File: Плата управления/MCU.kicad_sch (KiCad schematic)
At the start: 19 parts, among them U4 STM32F767VITx, U7 ASEMB-10

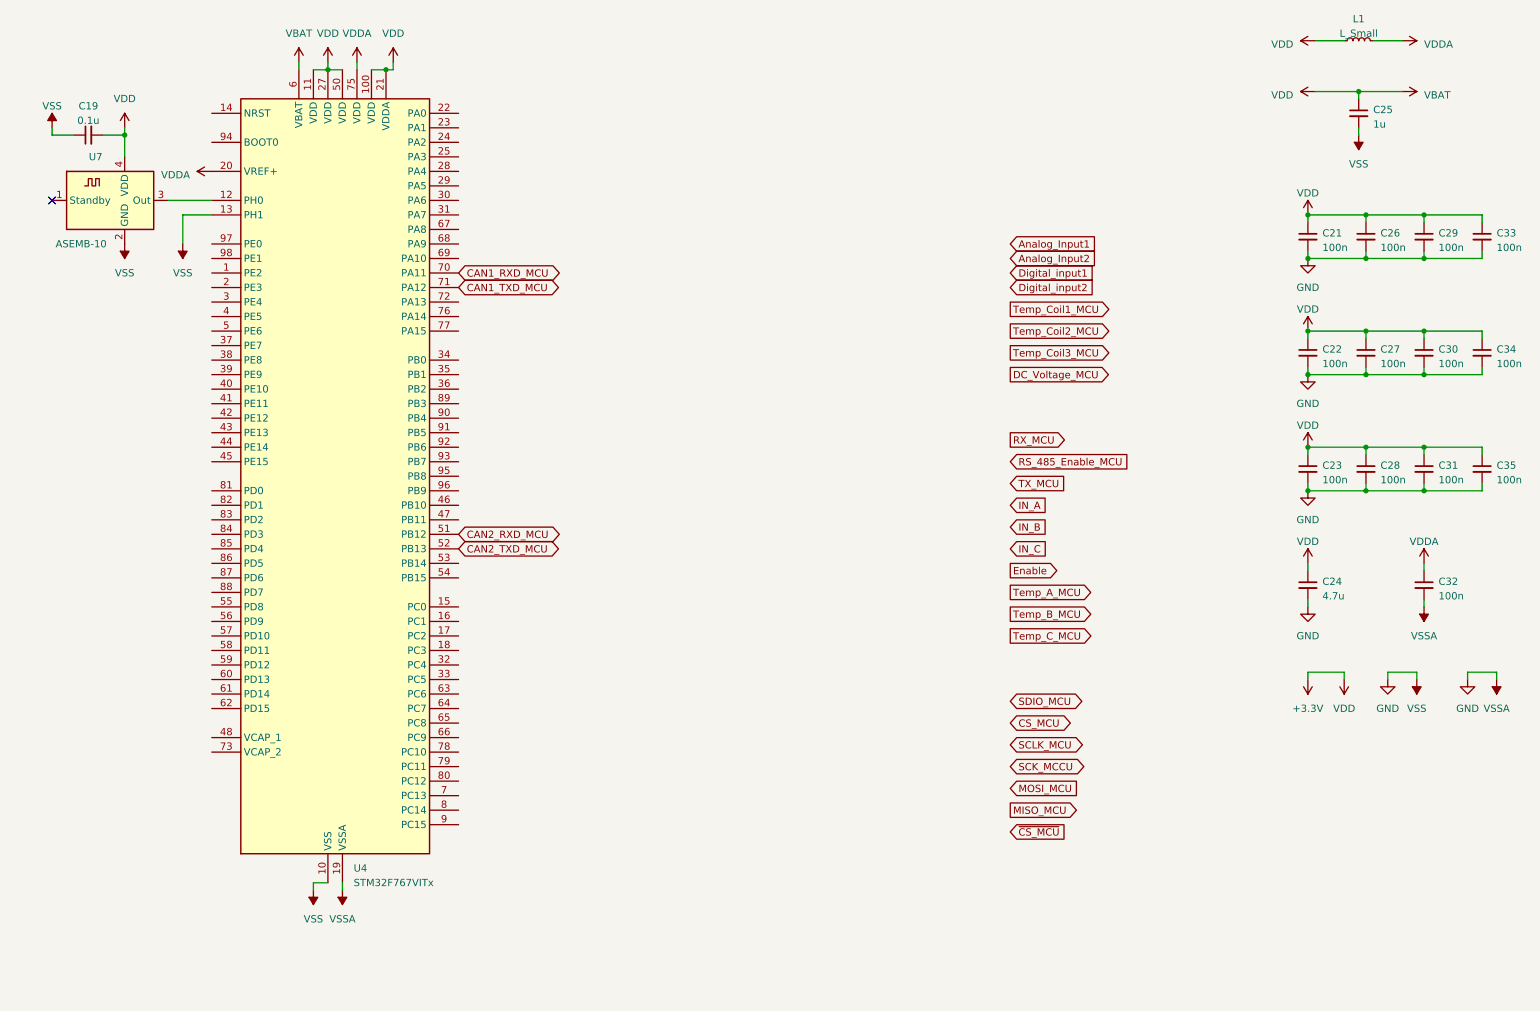
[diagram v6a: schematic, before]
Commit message: Заменил разъём под силовую плату
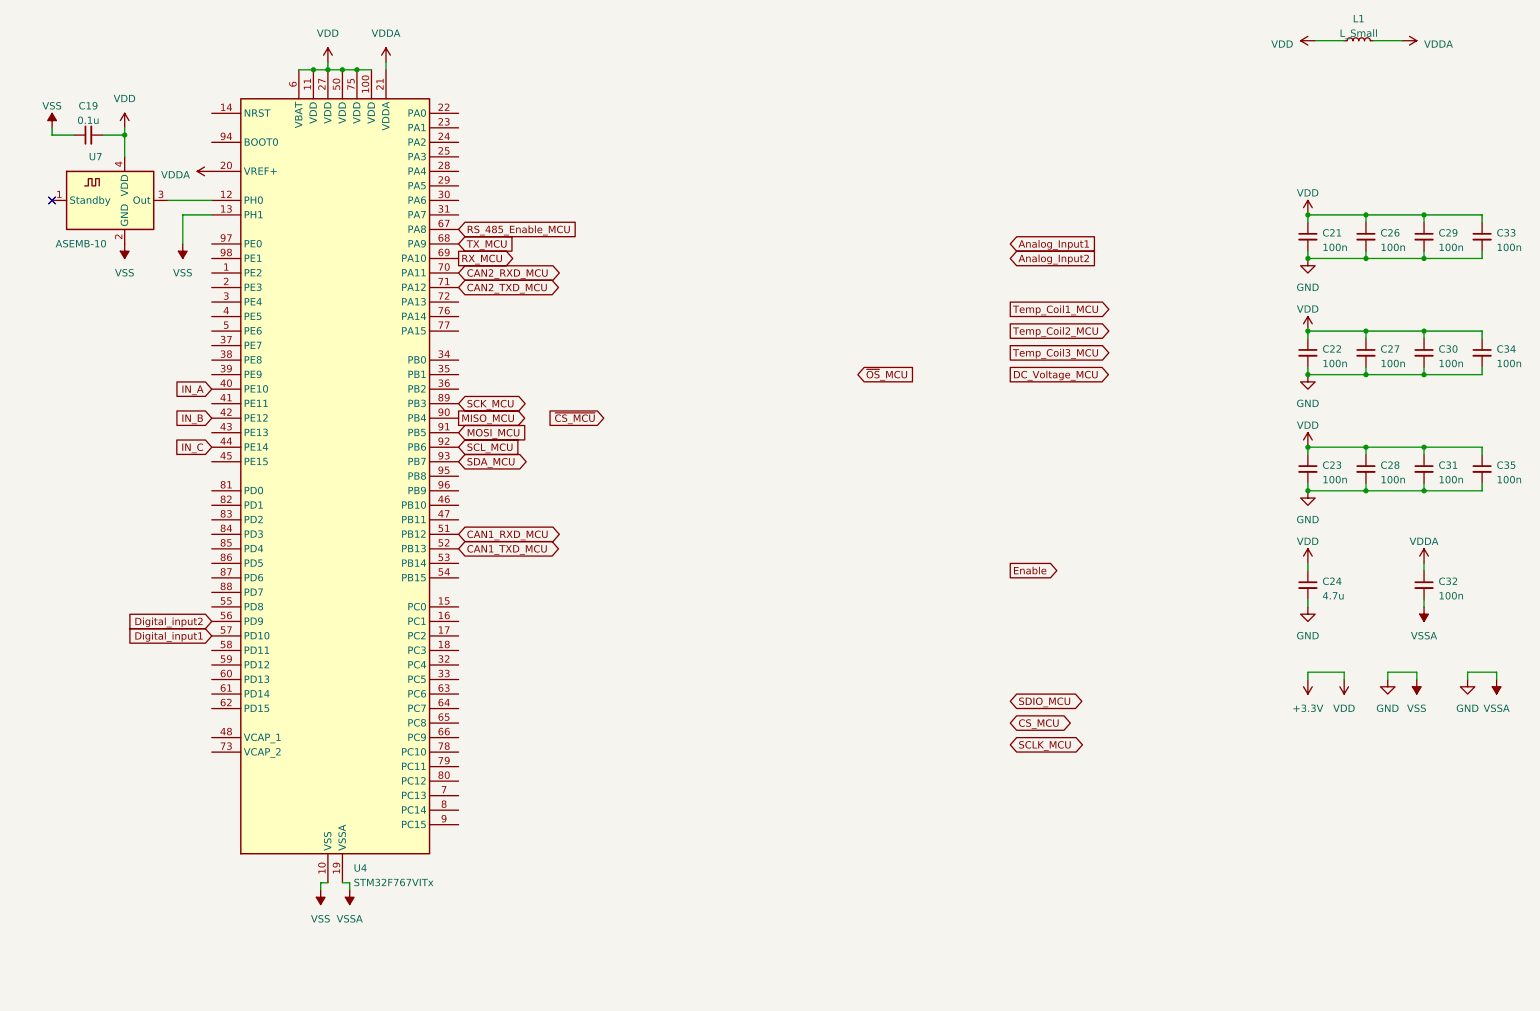
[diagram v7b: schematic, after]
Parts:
- removed C25: 1u, Capacitor_SMD:C_0603_1608Metric_Pad1.08x0.95mm_HandSolder, symbol Device:C_Small
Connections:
- net +3.3V: now also U4.75 (VDD); no longer U4.21 (VDDA)
- net CAN1_RXD_MCU: now also U4.51 (PB12); no longer U4.70 (PA11)
- net CAN1_TXD_MCU: now also U4.52 (PB13); no longer U4.71 (PA12)
- net CAN2_RXD_MCU: now also U4.70 (PA11); no longer U4.51 (PB12)
- net CAN2_TXD_MCU: now also U4.71 (PA12); no longer U4.52 (PB13)
- net Digital_input1: now also U4.57 (PD10)
- net Digital_input2: now also U4.56 (PD9)
- net IN_A: now also U4.40 (PE10)
- net IN_B: now also U4.42 (PE12)
- net IN_C: now also U4.44 (PE14)
- net MISO_MCU: now also U4.90 (PB4)
- net MOSI_MCU: now also U4.91 (PB5)
- net RS_485_Enable_MCU: now also U4.67 (PA8)
- net RX_MCU: now also U4.69 (PA10)
- net TX_MCU: now also U4.68 (PA9)
- net VDDA: now also U4.21 (VDDA); no longer U4.75 (VDD)
- net SCK_MCU: now reaches U4.89 (PB3)
- net SCL_MCU: now reaches U4.92 (PB6)
- net SDA_MCU: now reaches U4.93 (PB7)

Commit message: Разделил аналоговое и цифровое питание
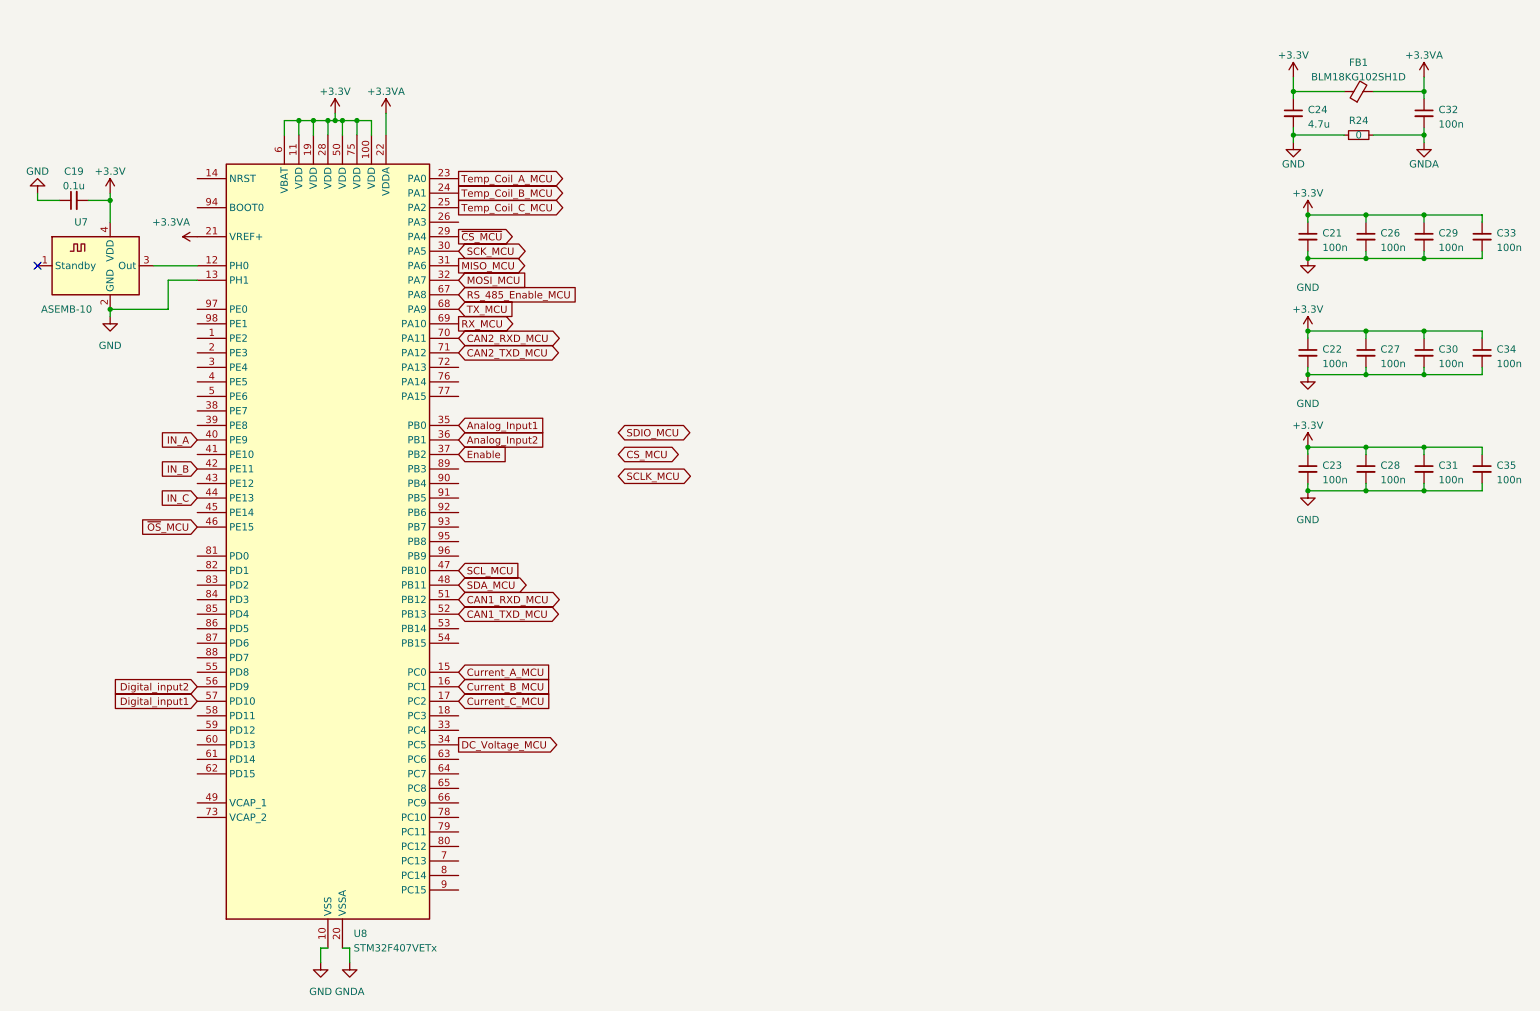
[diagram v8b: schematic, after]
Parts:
- removed L1: L_Small, symbol Device:L_Small
- removed U4: STM32F767VITx, Package_QFP:LQFP-100_14x14mm_P0.5mm, symbol MCU_ST_STM32F7:STM32F767VITx
- added FB1: BLM18KG102SH1D, Inductor_SMD:L_0603_1608Metric_Pad1.05x0.95mm_HandSolder, symbol Device:FerriteBead_Small
- added R24: 0, Resistor_SMD:R_0603_1608Metric_Pad0.98x0.95mm_HandSolder, symbol Device:R_Small
- added U8: STM32F407VETx, Package_QFP:LQFP-100_14x14mm_P0.5mm, symbol MCU_ST_STM32F4:STM32F407VETx
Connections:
- net +3.3V: now also FB1.1, U8.100 (VDD), U8.11 (VDD), U8.19 (VDD), U8.28 (VDD), U8.50 (VDD), U8.6 (VBAT), U8.75 (VDD)
- net Analog_Input1: now also U8.35 (PB0)
- net Analog_Input2: now also U8.36 (PB1)
- net CAN1_RXD_MCU: now also U8.51 (PB12)
- net CAN1_TXD_MCU: now also U8.52 (PB13)
- net CAN2_RXD_MCU: now also U8.70 (PA11)
- net CAN2_TXD_MCU: now also U8.71 (PA12)
- net DC_Voltage_MCU: now also U8.34 (PC5)
- net Digital_input1: now also U8.57 (PD10)
- net Digital_input2: now also U8.56 (PD9)
- net Enable: now also U8.37 (PB2)
- net GND: now also R24.1, U8.10 (VSS), U8.13 (PH1), U8.27 (VSS), U8.74 (VSS), U8.99 (VSS); no longer C32.2
- net IN_A: now also U8.40 (PE9)
- net IN_B: now also U8.42 (PE11)
- net IN_C: now also U8.44 (PE13)
- net MISO_MCU: now also U8.31 (PA6)
- net MOSI_MCU: now also U8.32 (PA7)
- net RS_485_Enable_MCU: now also U8.67 (PA8)
- net RX_MCU: now also U8.69 (PA10)
- net SCK_MCU: now also U8.30 (PA5)
- net SCL_MCU: now also U8.47 (PB10)
- net SDA_MCU: now also U8.48 (PB11)
- net TX_MCU: now also U8.68 (PA9)
- net ~{CS_MCU}: now also U8.29 (PA4)
- net ~{OS}_MCU: now also U8.46 (PE15)
- net at U7.3 (Out): now also U8.12 (PH0)
- net VDDA renamed +3.3VA
- net +3.3VA: now also FB1.2, U8.21 (VREF+), U8.22 (VDDA)
- new net Current_A_MCU: U8.15 (PC0)
- new net Current_B_MCU: U8.16 (PC1)
- new net Current_C_MCU: U8.17 (PC2)
- new net GNDA: C32.2, R24.2, U8.20 (VSSA)
- new net Temp_Coil_A_MCU: U8.23 (PA0)
- new net Temp_Coil_B_MCU: U8.24 (PA1)
- new net Temp_Coil_C_MCU: U8.25 (PA2)
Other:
- moved on the sheet: C19, C24, C32, U7
